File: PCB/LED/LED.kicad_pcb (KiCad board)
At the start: 2 copper layers, 70 x 70 mm, 31 parts, among them J1 Reset, J2 Wago, J3 TC2030-USB-NL-DS, J5 USB-C-Socket-H, T1 T3902_MEMS_Mic, U6 ESP32-S3-MINI-1, U7 MD8942

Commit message: Slopt
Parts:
- moved T1 0.05 mm to (117.4, 95.7)

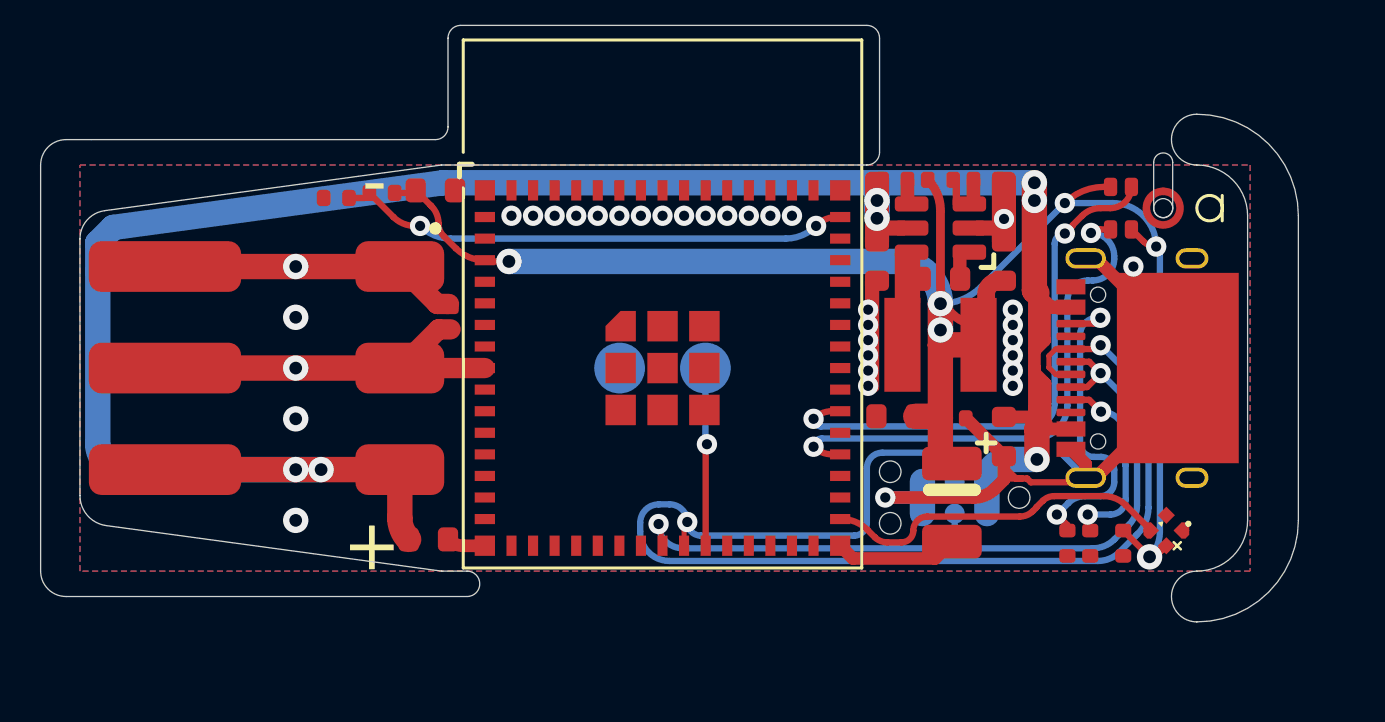
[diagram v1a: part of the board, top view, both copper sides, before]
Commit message: New microphone
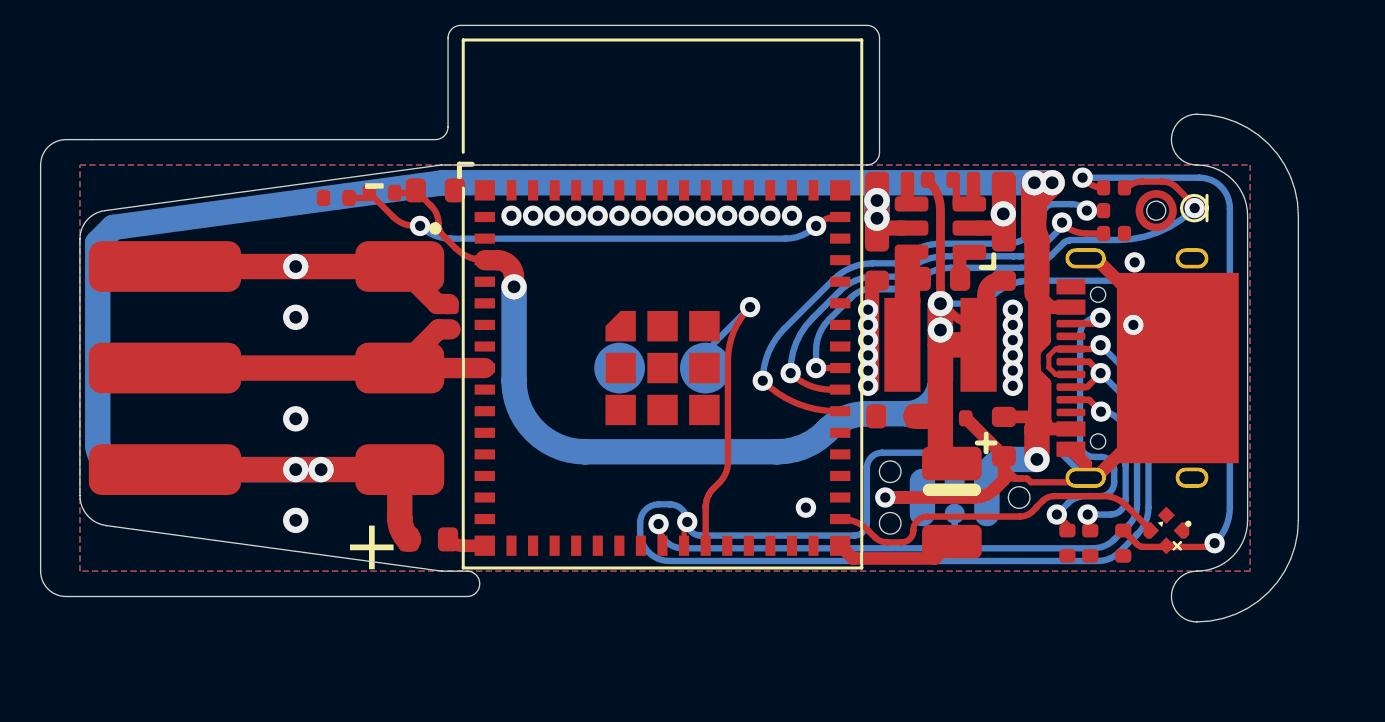
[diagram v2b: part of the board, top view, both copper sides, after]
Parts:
- removed T1: T3902_MEMS_Mic, RevK:T3902_MEMS_Mic
- added ICS1: ICS43434_MEMS_Mic, RevK:ICS43434_MEMS_Mic, F.Cu at (117.1, 95.8)
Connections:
- U6 pad 34: DATA -> unconnected-(U6-GPIO38-Pad34)
- U6 pad 36: CLK -> SD
- U6 pad 37: unconnected-(U6-GPIO41-Pad37) -> WS
- U6 pad 38: unconnected-(U6-GPIO42-Pad38) -> SCK
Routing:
- net SCK: track 0.00 -> 23.9 mm, vias 0 -> 2
- net CLK: track 21.6 -> 0.00 mm, vias 2 -> 0
- net DATA: track 21.2 -> 0.00 mm, vias 2 -> 0
- net SD: track 0.00 -> 20.2 mm, vias 0 -> 2
- net WS: track 0.00 -> 17.5 mm, vias 0 -> 2
- net +3V3: track 63.1 -> 77.9 mm, vias 6 -> 5
- net Net-(J1-Pin_2): track 7.05 -> 12.9 mm
- net DC: track 93.6 -> 97.6 mm
- net LED: vias 1 -> 0
- net GND: vias 33 -> 35
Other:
- board text added: "C42"
- board text added: "D40"
- board text added: "W41"
- board text removed: "C40"
- board text removed: "D38"
- board text removed: "PDM"

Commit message: tweak
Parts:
- removed ICS1: ICS43434_MEMS_Mic, RevK:ICS43434_MEMS_Mic
- added C8: 100nF, RevK:C_0402, F.Cu at (120.7, 96.2)
- added U1: ICS43434_MEMS_Mic, RevK:ICS43434_MEMS_Mic, F.Cu at (117.1, 95.8)
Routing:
- net GND: track 45.6 -> 48.1 mm
- net +3V3: track 77.9 -> 78.6 mm, vias 5 -> 6

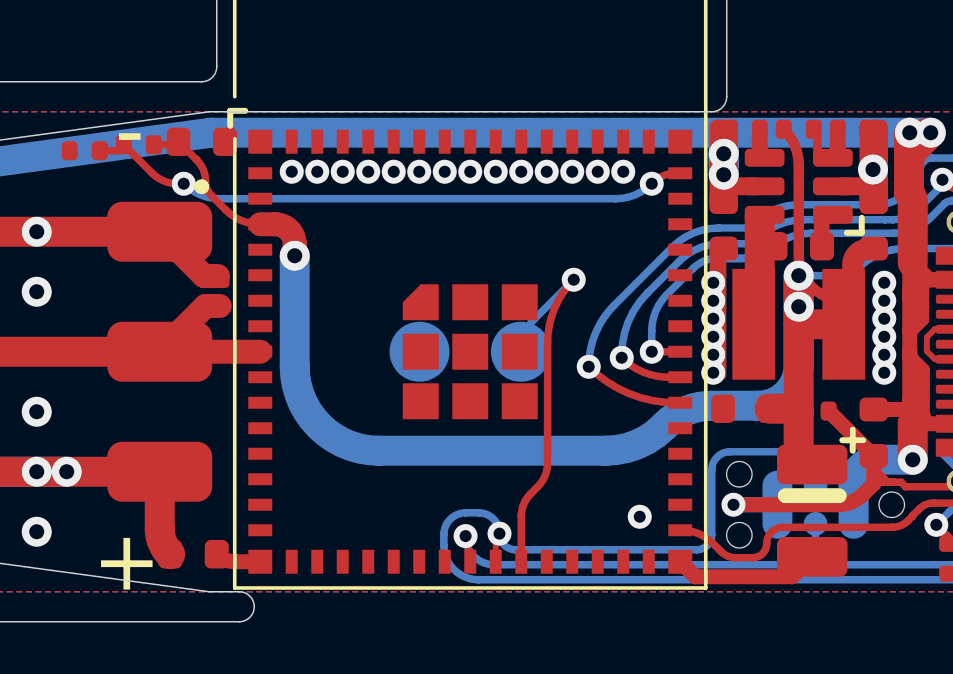
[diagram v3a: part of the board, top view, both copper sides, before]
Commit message: Pads for button
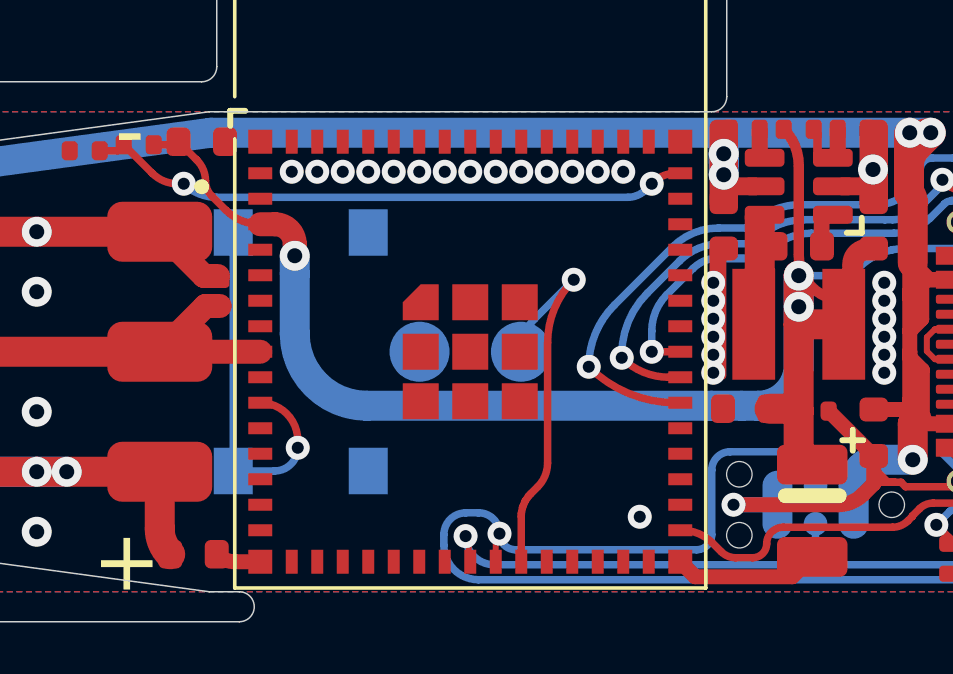
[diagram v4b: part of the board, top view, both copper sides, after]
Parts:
- added SW1: Button, RevK:SW_Push_1P1T_NO_6x6mm, B.Cu at (92.8, 102.0)
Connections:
- U6 pad 10: unconnected-(U6-GPIO6-Pad10) -> PUSH
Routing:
- net PUSH: track 0.00 -> 12.7 mm, vias 0 -> 1
- net +3V3: track 78.6 -> 76.9 mm
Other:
- board text added: "(5V WHEN USB)"
- board text added: "4V-35V POWER"
- board text added: "6"
- board text added: "HomeIsWhereTheSmartIs"
- board text added: "Made in China"
- board text removed: "4V-35V POWER (5V WHEN USB)"
- board text removed: "5060634238090"
- board text removed: "HomeIsWhereTheSmartIs Made in China"

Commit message: ADC
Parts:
- added R1: 124K, RevK:R_0402, F.Cu at (87.4, 106.9)
- added R3: 10K, RevK:R_0402, F.Cu at (85.6, 106.7)
- moved C1 2.00 mm to (109.8, 105.3)
- moved C10 2.00 mm to (106.9, 95.8)
- moved C11 2.00 mm to (111.9, 95.8)
- moved C12 2.00 mm to (109.4, 96.5)
- moved C2 2.00 mm to (109.9, 102.0)
- moved C3 2.00 mm to (107.7, 101.9)
- moved C4 2.00 mm to (116.6, 106.9)
- moved C5 2.00 mm to (111.9, 102.7)
- moved C7 2.00 mm to (89.5, 93.0)
- moved C8 2.00 mm to (120.7, 94.2)
- moved C9 2.00 mm to (85.6, 93.3)
- moved D1 2.00 mm to (118.3, 106.4)
- moved D2 2.00 mm to (90.1, 98.0)
- moved J1 2.00 mm to (98.5, 100.0)
- moved J2 2.00 mm to (83.5, 100.0)
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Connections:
- U6 pad 15: unconnected-(U6-GPIO11-Pad15) -> ADC
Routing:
- net ADC: track 0.00 -> 8.44 mm, vias 0 -> 2
- net DC: track 97.4 -> 98.6 mm
- net LED: vias 0 -> 1
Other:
- board text added: "11"

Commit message: Tidy
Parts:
- moved SW1 0.90 mm to (91.9, 100.0)
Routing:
- net PUSH: track 12.7 -> 9.43 mm
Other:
- board text added: "I2S"
- board text added: "led.revk.uk"

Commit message: Level shift
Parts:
- removed D2: ~, RevK:DFN1006-2L
- added D3: 5V, RevK:D_SOD-523, F.Cu at (90.0, 98.0)
- added R7: 124K, RevK:R_0402, F.Cu at (90.0, 102.0)
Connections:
- U6 pad 12: unconnected-(U6-GPIO8-Pad12) -> ADC
- U6 pad 15: ADC -> unconnected-(U6-GPIO11-Pad15)
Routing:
- net ADC: track 8.44 -> 11.5 mm
- net PUSH: track 9.43 -> 12.0 mm
- net DC: track 98.6 -> 101.1 mm
- net LED: track 15.2 -> 17.4 mm
- net +3V3: track 76.9 -> 76.1 mm

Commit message: No level convert
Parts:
- removed D3: 5V, RevK:D_SOD-523
- removed R7: 124K, RevK:R_0402
- added D2: ~, RevK:DFN1006-2L, F.Cu at (89.8, 98.0)
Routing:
- net LED: track 17.4 -> 14.9 mm
- net DC: track 101.1 -> 98.6 mm
